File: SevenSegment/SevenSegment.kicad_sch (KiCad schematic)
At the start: 11 parts, among them IC1 CD4033BE, IC2 CD4033BE, J1 Conn_01x04

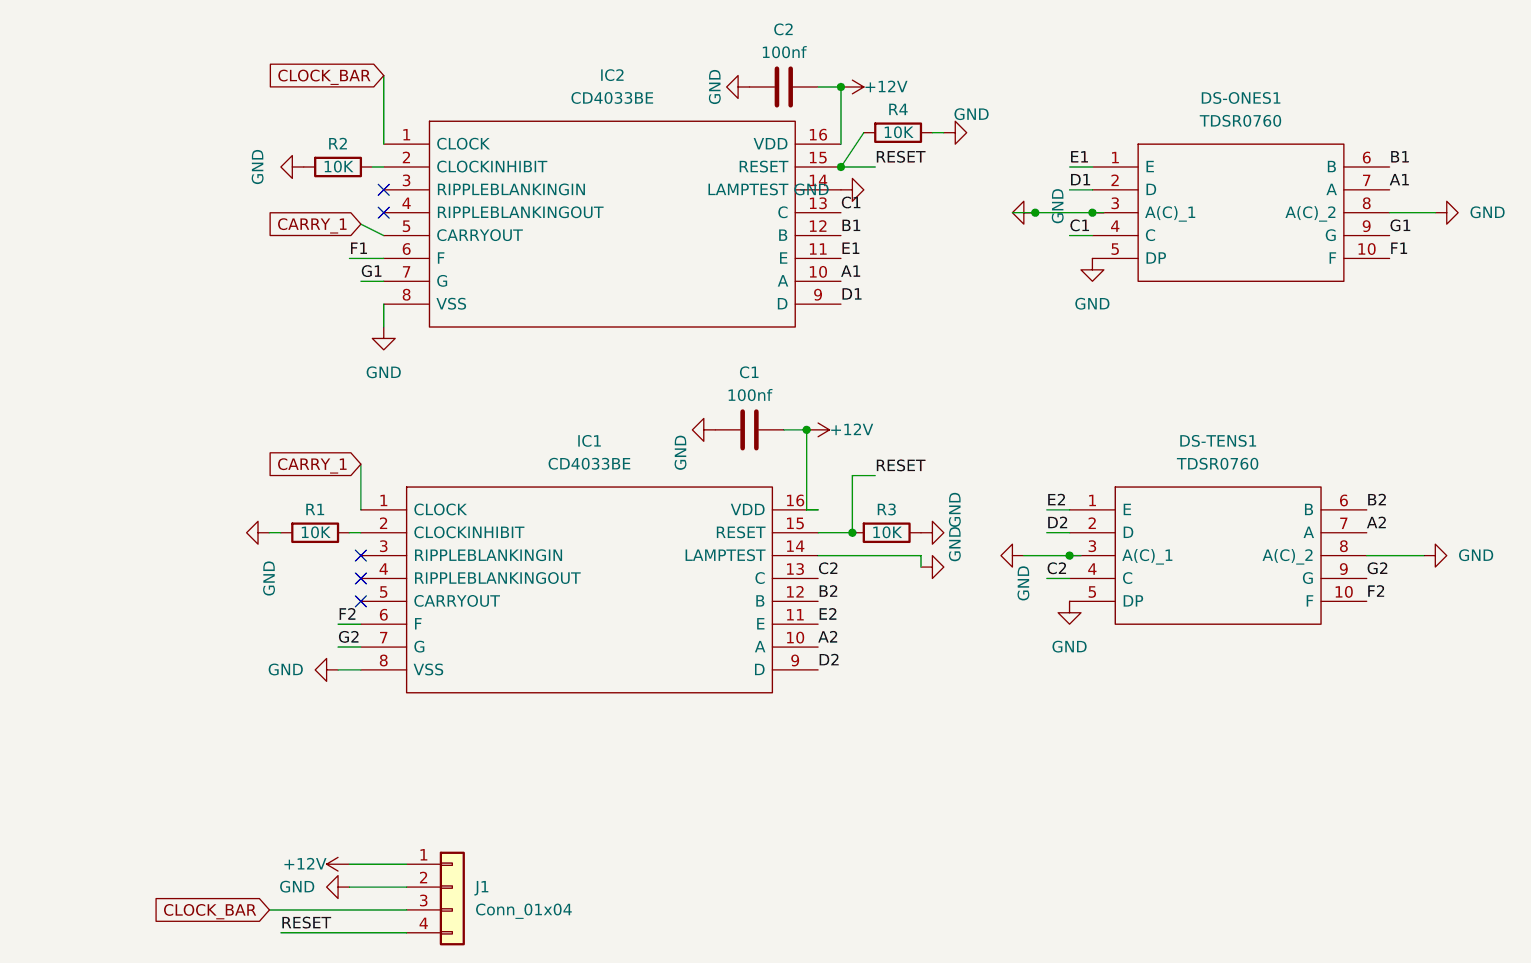
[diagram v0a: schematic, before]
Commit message: Layout SevenSegment Board. Nano Schematic
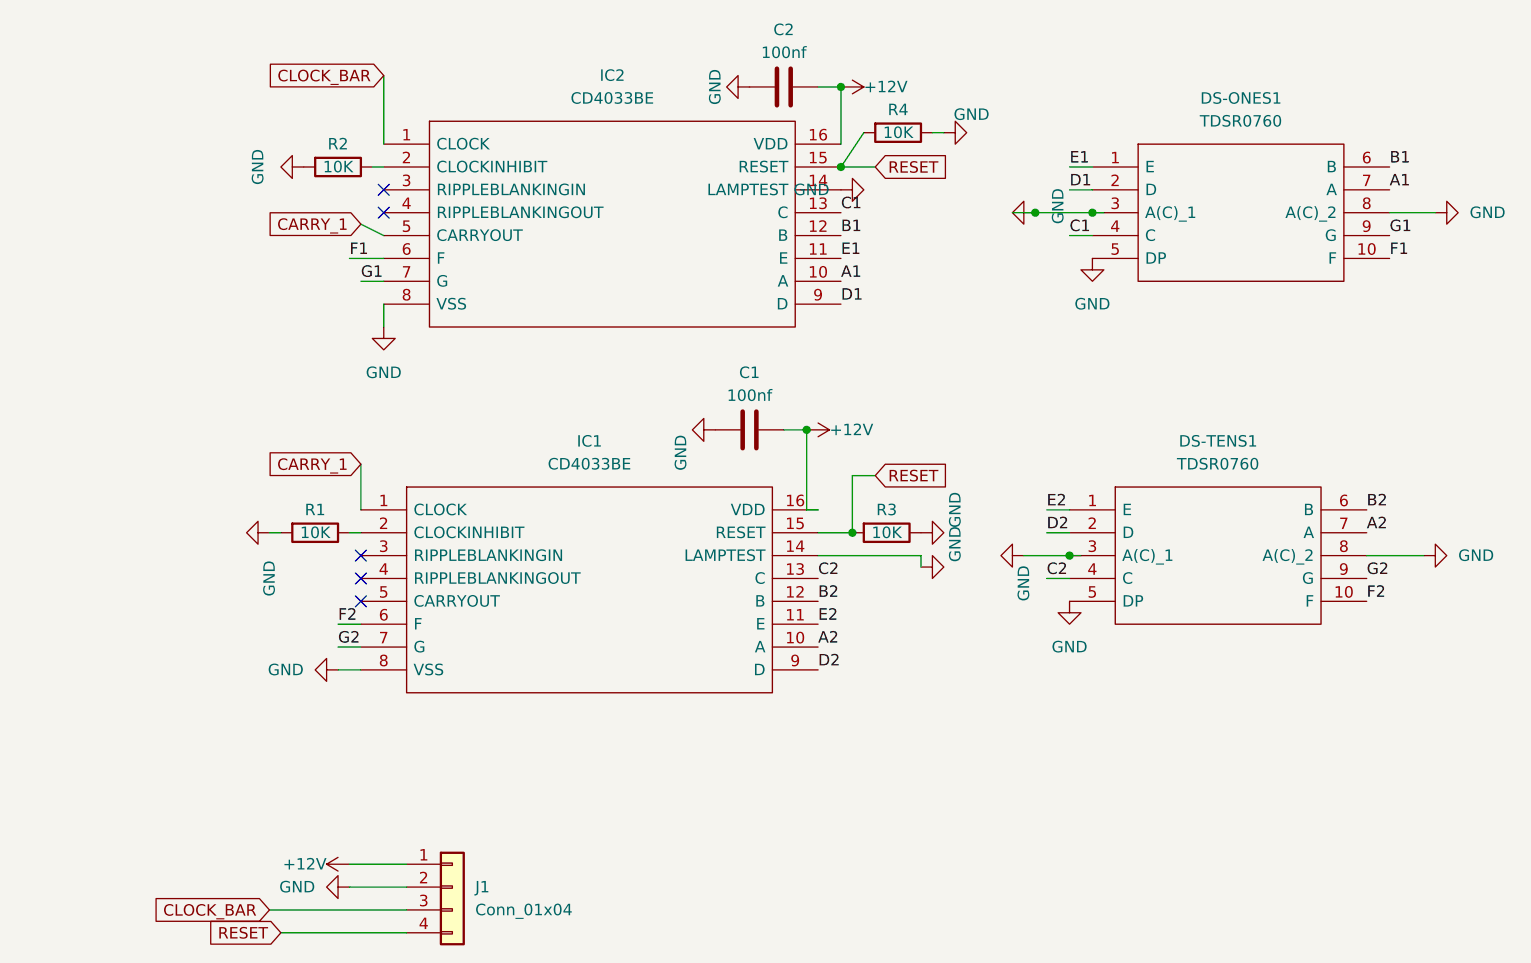
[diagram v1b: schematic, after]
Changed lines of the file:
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@@
-    (effects (font (size 1.27 1.27)) (justify left bottom))
-  )
-  (label "RESET" (at 140.97 66.04 0)
     (effects (font (size 1.27 1.27)) (justify left bottom))
   )
@@
     (effects (font (size 1.27 1.27)) (justify left bottom))
   )
-  (label "RESET" (at 74.93 151.13 0)
-    (effects (font (size 1.27 1.27)) (justify left bottom))
-  )
   (label "G1" (at 83.82 78.74 0)
     (effects (font (size 1.27 1.27)) (justify left bottom))
@@
     (effects (font (size 1.27 1.27)) (justify left bottom))
   )
-  (label "RESET" (at 140.97 100.33 0)
-    (effects (font (size 1.27 1.27)) (justify left bottom))
-  )
   (label "D1" (at 137.16 81.28 0)
     (effects (font (size 1.27 1.27)) (justify left bottom))
@@
     (effects (font (size 1.27 1.27)) (justify left bottom))
   )
+  (global_label "RESET" (shape input) (at 140.97 100.33 0) (fields_autoplaced)
+    (effects (font (size 1.27 1.27)) (justify left))
+    (property "Intersheet References" "${INTERSHEET_REFS}" (id 0) (at 149.1283 100.4094 0)
+      (effects (font (size 1.27 1.27)) (justify left) hide)
+    )
+  )
   (global_label "CLOCK_BAR" (shape input) (at 86.36 55.88 180) (fields_autoplaced)
     (effects (font (size 1.27 1.27)) (justify right))
     (property "Intersheet References" "${INTERSHEET_REFS}" (id 0) (at 73.1821 55.9594 0)
       (effects (font (size 1.27 1.27)) (justify right) hide)
+    )
+  )
+  (global_label "RESET" (shape input) (at 140.97 66.04 0) (fields_autoplaced)
+    (effects (font (size 1.27 1.27)) (justify left))
+    (property "Intersheet References" "${INTERSHEET_REFS}" (id 0) (at 149.1283 66.1194 0)
+      (effects (font (size 1.27 1.27)) (justify left) hide)
     )
   )
@@
       (effects (font (size 1.27 1.27)) (justify right) hide)
     )
+  )
+  (global_label "RESET" (shape input) (at 74.93 151.13 180) (fields_autoplaced)
+    (effects (font (size 1.27 1.27)) (justify right))
+    (property "Intersheet References" "${INTERSHEET_REFS}" (id 0) (at 66.7717 151.0506 0)
+      (effects (font (size 1.27 1.27)) (justify right) hide)
+    )

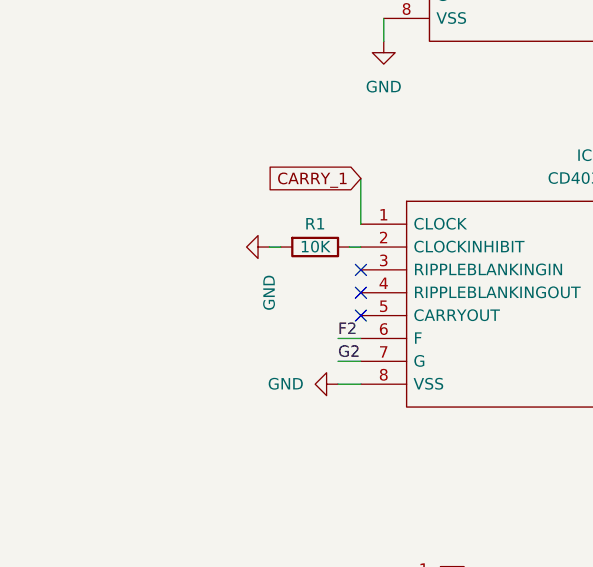
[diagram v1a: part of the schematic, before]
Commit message: Update TODOs in SevenSegment
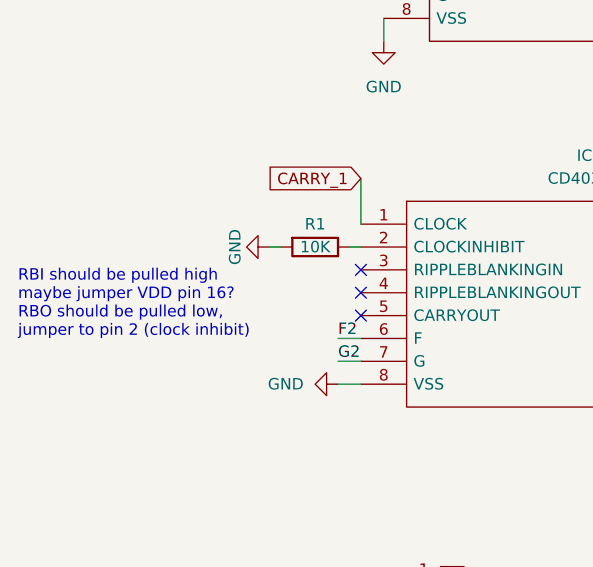
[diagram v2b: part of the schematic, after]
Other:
- note added: "RBI should be pulled high maybe jumper VDD pin 16? RBO should be pulled low, jumper to pin 2 (clock inhibit)"
